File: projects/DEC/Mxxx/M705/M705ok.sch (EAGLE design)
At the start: 48 parts

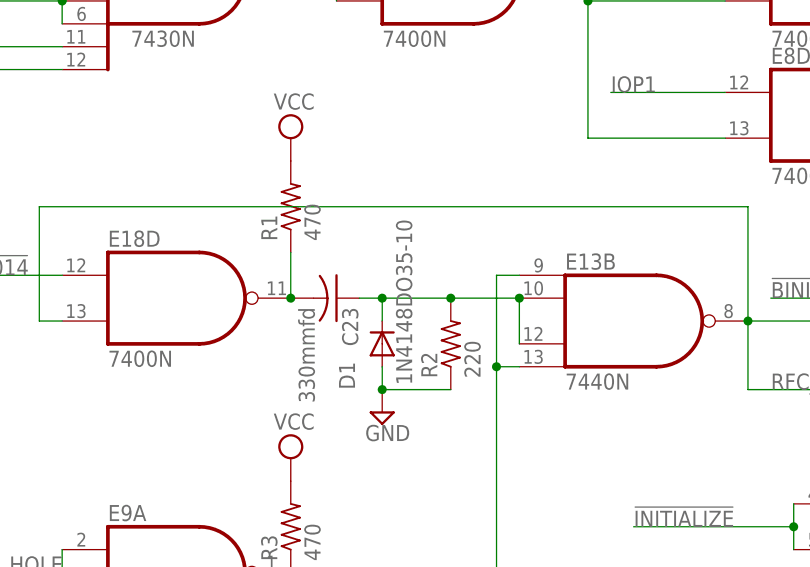
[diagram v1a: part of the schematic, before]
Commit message: Fix damage caused by update when 1N4148 was encountered without a value set.
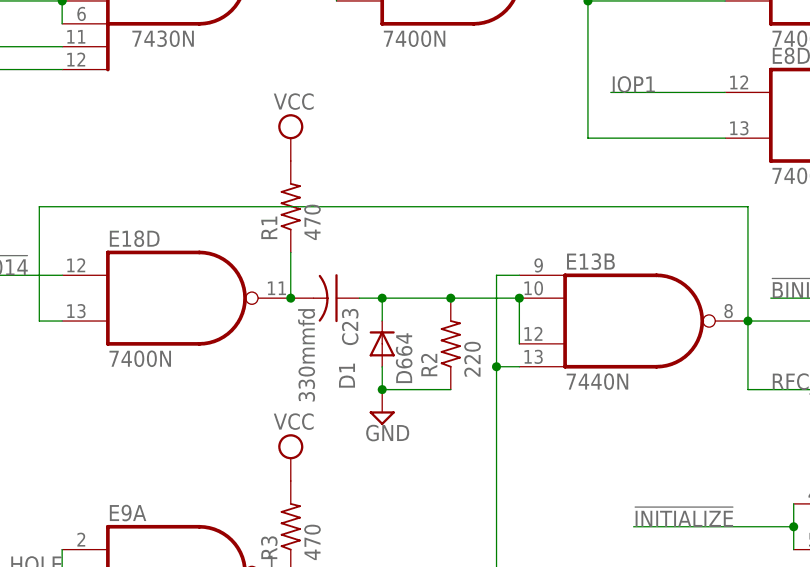
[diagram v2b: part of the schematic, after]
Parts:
- D1: value 1N4148DO35-10 -> D664
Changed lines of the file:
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@@
 <part name="V3" library="supply2" deviceset="VCC" device=""/>
 <part name="C23" library="rcl" deviceset="C-US" device="050-025X075" value="330mmfd"/>
-<part name="D1" library="diode" deviceset="1N4148" device="DO35-10"/>
+<part name="D1" library="diode" deviceset="1N4148" device="DO35-10" value="D664"/>
 <part name="V7" library="supply2" deviceset="GND" device=""/>
 <part name="R2" library="rcl" deviceset="R-US_" device="0207/10" value="220"/>
